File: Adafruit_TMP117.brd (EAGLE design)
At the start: 25.4 x 17.8 mm, 20 parts, among them X1 TMP117_WSON

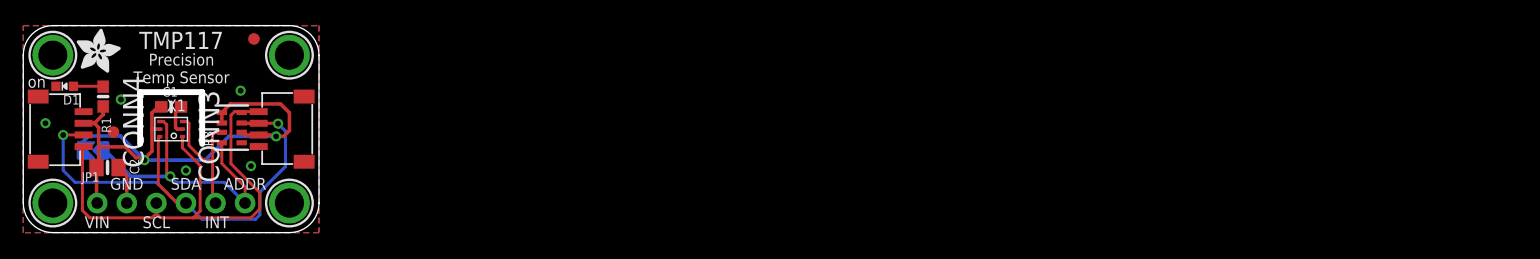
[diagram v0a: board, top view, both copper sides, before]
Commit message: changed in to a smaller layout with a "finger" and single connector
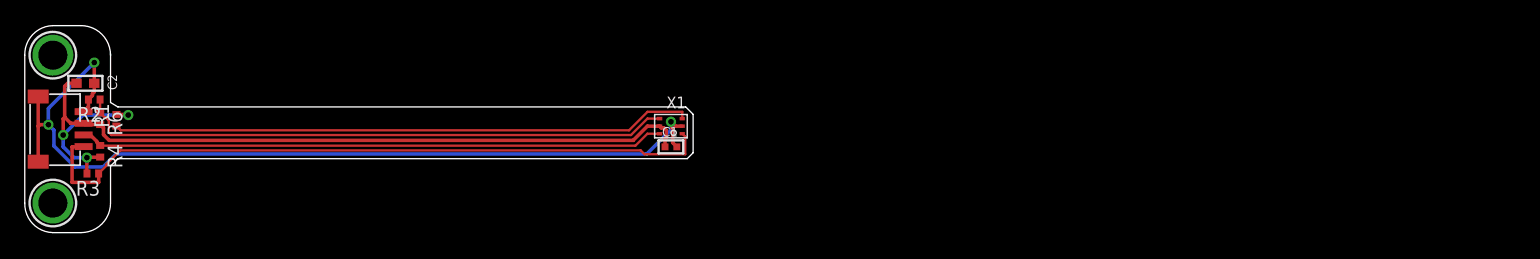
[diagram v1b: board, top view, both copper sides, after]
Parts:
- removed CONN3: STEMMA_I2C_QT, microbuilder:JST_SH4
- removed D1: GREEN, microbuilder:CHIPLED_0603_NOOUTLINE
- removed FID3, FID4: FIDUCIAL_1MM, microbuilder:FIDUCIAL_1MM
- removed JP1: (no value), microbuilder:1X06_ROUND_70
- removed SJ1: (no value), microbuilder:SOLDERJUMPER_ARROW_NOPASTE
- removed U$17, U$21: MOUNTINGHOLE2.5, microbuilder:MOUNTINGHOLE_2.5_PLATED
- removed U$22: (no value), microbuilder:ADAFRUIT_3.5MM
- removed U$25: (no value), microbuilder:PCBFEAT-REV-040
- removed U$30, U$31: (no value), silks:STEMMAQT
- added R2, R4: 10k, rcl:R0402
- added R6: 0R, rcl:R0402
- C1: device microbuilder:0603-NO -> microbuilder:_0402
- C2: device microbuilder:0805-NO -> microbuilder:_0603
- R1: value (none) -> 10k; device microbuilder:0603-NO -> rcl:R0402
- R3: value 10K -> 10k; device microbuilder:RESPACK_4X0603 -> rcl:R0402
- moved C1 43.1 mm to (55.6, 7.37)
- moved X1 42.9 mm to (55.6, 9.14)
- moved R3 12.6 mm to (5.97, 5.08), turned to 180 degrees
- moved C2 7.49 mm to (5.33, 12.8)
- moved R1 2.33 mm to (8.00, 9.65), turned to 90 degrees
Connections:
- removed net N$1: D1.A, R1.1
- net ADDR: now also R2.1, R6.1; no longer JP1.6, R3.8, SJ1.1
- net GND: now also R2.2; no longer CONN3.1, CONN3.MT1, CONN3.MT2, D1.C, JP1.2, R3.1
- net INT: now also R1.1; no longer JP1.5, R3.7
- net SCL: now also R3.1; no longer CONN3.4, JP1.3, R3.4
- net SDA: now also R4.1; no longer CONN3.3, JP1.4, R3.3
- net VCC: now also R4.2, R6.2; no longer CONN3.2, JP1.1, R3.5, R3.6, SJ1.2
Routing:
- net GND: track 5.96 -> 79.3 mm, vias 5 -> 3
- net INT: track 11.9 -> 50.0 mm
- net ADDR: track 25.2 -> 51.2 mm, vias 1 -> 0
- net VCC: track 52.8 -> 73.6 mm, vias 2 -> 3
- net SCL: track 42.1 -> 60.4 mm
- net SDA: track 42.9 -> 50.3 mm, vias 2 -> 0
- net N$1: track 2.57 -> 0.00 mm
- removed copper zone on layer 1, net GND
- removed copper zone on layer 16, net GND
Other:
- board size 25.4 x 17.8 mm -> 57.4 x 17.8 mm
- board text removed: "ADDR"
- board text removed: "Default I2C addr 0x48"
- board text removed: "GND"
- board text removed: "INT"
- board text removed: "Precision Temp Sensor"
- board text removed: "SCL"
- board text removed: "SDA"
- board text removed: "TMP117"
- board text removed: "Temperature Sensor"
- board text removed: "VCC"
- board text removed: "VIN"
- board text removed: "VLogic/Vcc: 3-5VDC"
- board text removed: "on"
- board text removed: "±0.1°C@ 20-50"
- board text removed: "±0.3°C@ -55-150"

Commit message: new version, sensors on bottom side, connector on top side. Two sensors with I2C in series.
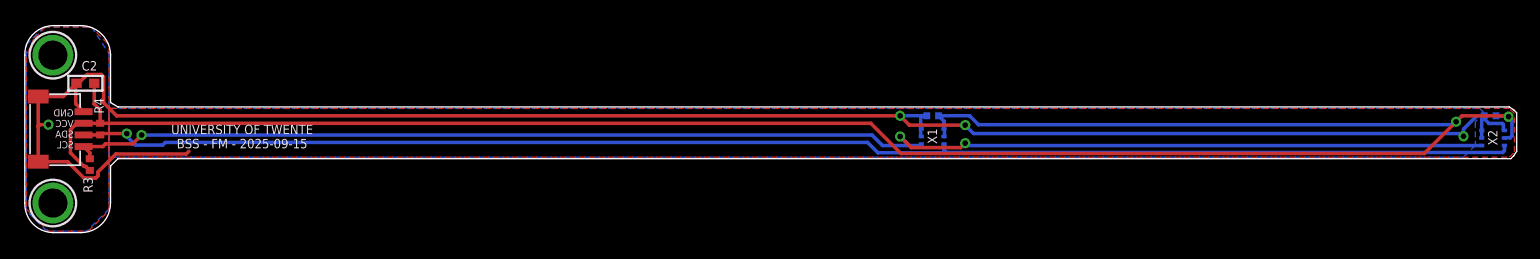
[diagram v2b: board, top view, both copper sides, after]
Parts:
- removed R1, R2: 10k, rcl:R0402
- removed R6: 0R, rcl:R0402
- added C3: 0.1uF, microbuilder:_0402
- added X2: TMP117_WSON, adafruit_sensor:WSON-6
- moved C1 22.6 mm to (78.1, 10.0), flipped to the bottom
- moved X1 22.5 mm to (78.1, 8.26), flipped to the bottom
- moved R4 1.91 mm to (6.60, 8.89), turned to 90 degrees
- moved R3 0.80 mm to (5.71, 5.84), turned to 270 degrees
- turned C2 to 180 degrees
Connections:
- removed net ADDR: R2.1, R6.1, X1.4
- removed net INT: R1.1, X1.3
- net GND: now also C3.2, X1.3, X2.2, X2.3, X2.4; no longer R2.2
- net SCL: now also X2.1
- net SDA: now also X2.6
- net VCC: now also C3.1, X1.4, X2.5; no longer R1.2, R6.2
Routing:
- net VCC: track 73.6 -> 185.9 mm, vias 3 -> 2
- net GND: track 79.3 -> 162.9 mm, vias 3 -> 4
- net SDA: track 50.3 -> 124.4 mm, vias 0 -> 1
- net SCL: track 60.4 -> 125.7 mm, vias 0 -> 3
- net ADDR: track 51.2 -> 0.00 mm
- net INT: track 50.0 -> 0.00 mm
- added copper zone on layer 1, net GND
- added copper zone on layer 16, net GND
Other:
- board size 57.4 x 17.8 mm -> 128.1 x 17.8 mm
- board text added: "GND VCC SDA SCL"
- board text added: "TMP117 - I2C: X1: ADD0=VCC X2: ADD0=GND"
- board text added: "UNIVERSITY OF TWENTE BSS - FM - 2025-09-15"
- board text added: "X1"
- board text added: "X2"
